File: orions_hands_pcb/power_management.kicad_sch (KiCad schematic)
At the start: 23 parts, among them Q2 AO3401A, U4 BQ24074RGT, U4 TPS63060

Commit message: title sync across sheets
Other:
- title: (none) -> Orions Hands
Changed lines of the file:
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@@
 (kicad_sch (version 20230121) (generator eeschema)
   (paper "A4")
+  (title_block
+    (title "Orions Hands")
+    (rev "2")
+  )
   (junction (at 99.06 68.58) (diameter 0) (color 0 0 0 0)
   )

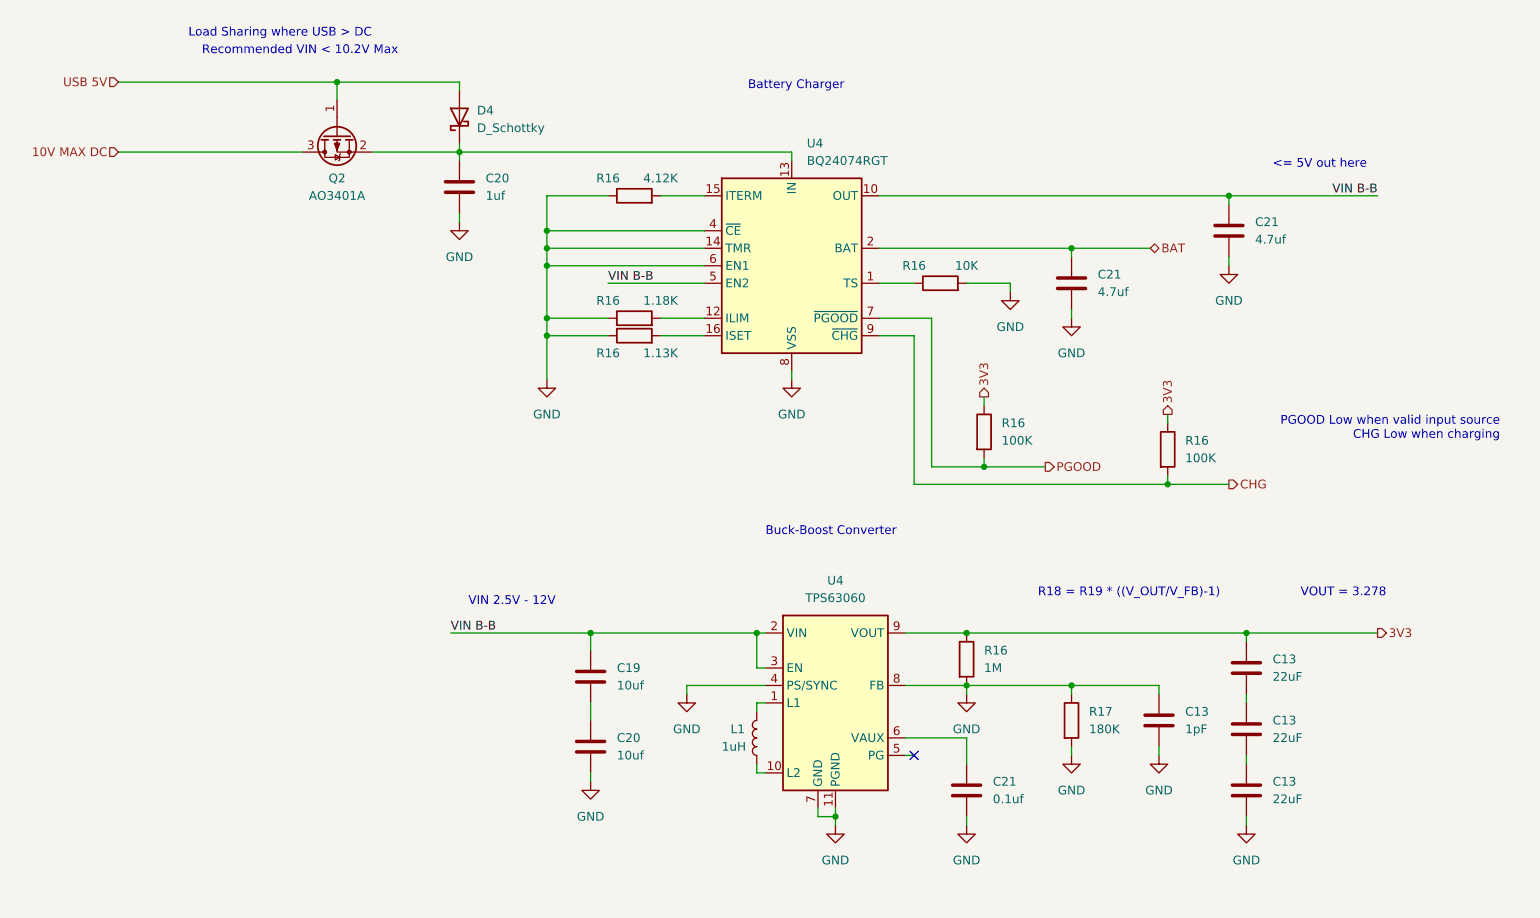
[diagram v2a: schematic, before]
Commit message: corrected power management
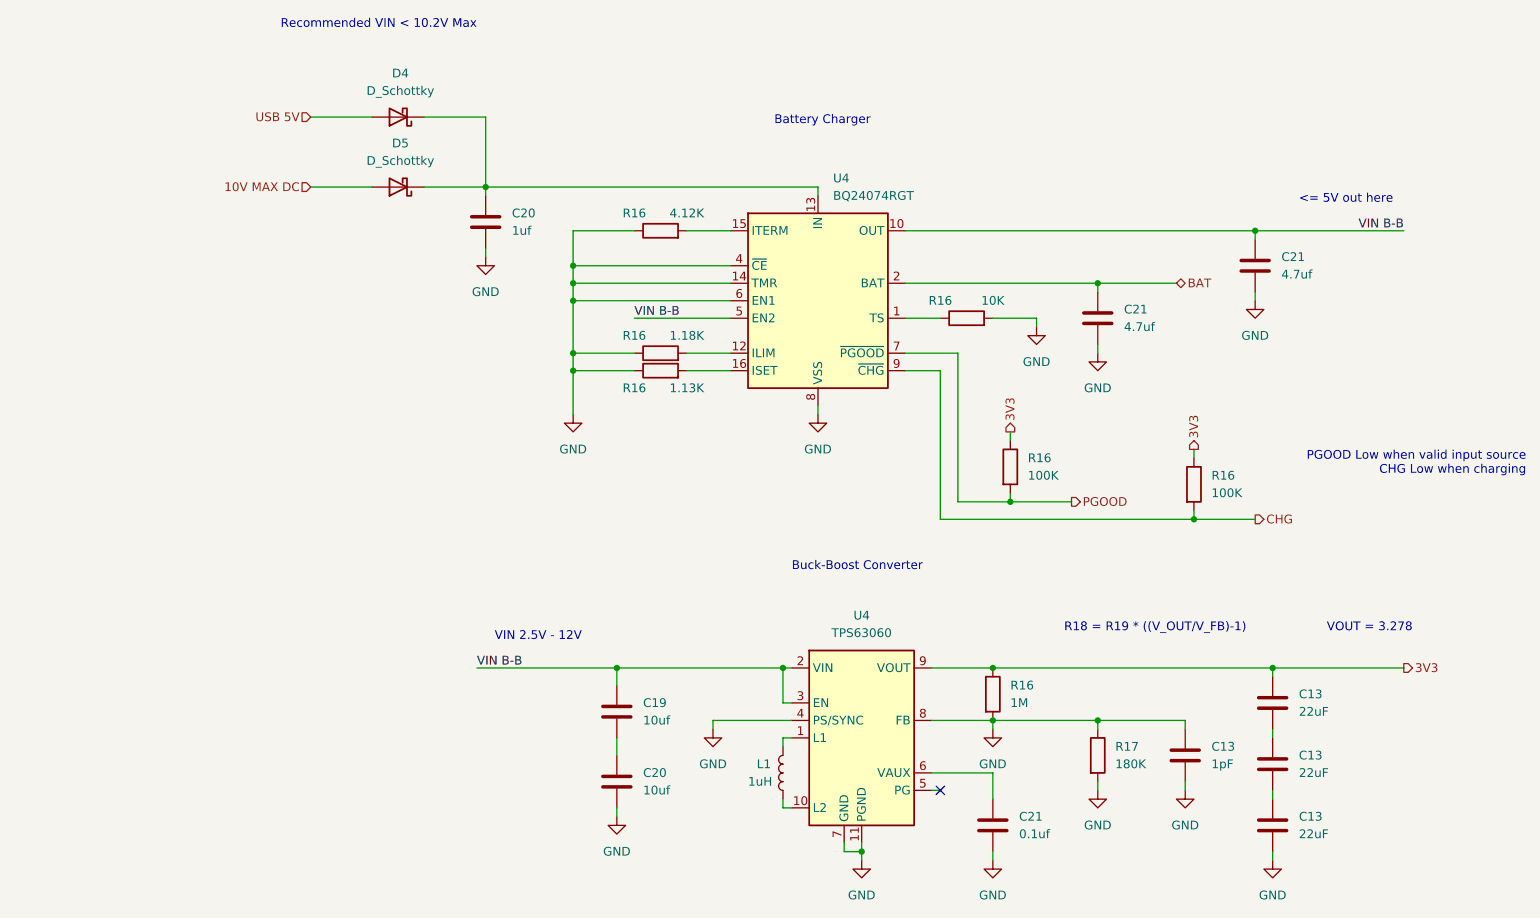
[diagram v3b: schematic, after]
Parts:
- removed Q2: AO3401A, Package_TO_SOT_SMD:SOT-23, symbol Transistor_FET:AO3401A
- added D5: D_Schottky, symbol Device:D_Schottky
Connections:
- net 10V MAX DC: now also D5.2 (A)
- net at C20.1, D4.1 (K), U4.13 (IN): now also D5.1 (K)
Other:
- note removed: "Load Sharing where USB > DC"
- moved on the sheet: C13, C19, C20, C21, D4, L1, R16, R17, U4

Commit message: typo correction
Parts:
- renumbered C20 to C15, C21 to C16, C21 to C19, C19 to C26, C20 to C27, C21 to C28, C13 to C29, C13 to C30, C13 to C31, C13 to C32, L1 to L2, R16 to R17, R16 to R18, R17 to R19, R16 to R20, R16 to R21, R16 to R22, R16 to R23, U4 to U5
